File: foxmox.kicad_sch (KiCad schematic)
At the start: 0 parts

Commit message: Fully transcribed PDF scan
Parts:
- added C1, C2: 27pF, symbol Device:C_Small_US
- added C3: .1uF, symbol Device:C_Small_US
- added C4: 1uF, symbol Device:C_Small_US
- added D1: 6.2V, Diode_SMD:D_MiniMELF, symbol Diode:BZV55B6V2
- added P1: 2.5mm plug, symbol Connector_Audio:AudioJack3
- added Q1: 2N2222A, symbol Device:Q_NPN
- added R1, R3: 20k, symbol Device:R_US
- added R2: 5k, symbol Device:R_Potentiometer_Trim_US
- added R4: 2.7k, symbol Device:R_US
- added R5: 10k, symbol Device:R_US
- added S1, S2: SW Hex-4, Button_Switch_SMD:Nidec_Copal_SH-7040B, symbol Switch:SW_Coded_SH-7080
- added S3: SPDT, symbol Switch:SW_SPDT
- added U1: PIC16F84, symbol MCU_Microchip_PIC16:PIC16F84-XXP
- added Y1: 3.579MHz, symbol Device:Crystal
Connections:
- new net: Q1.B, R3.2
- new net: Q1.C, R4.1
- new net: C3.1, D1.1 (K), S3.2 (B), U1.14 (VDD), U1.4 (~{MCLR})
- new net: R5.2, U1.1 (RA2)
- new net: S2.1, U1.10 (RB4)
- new net: S2.2, U1.11 (RB5)
- new net: S2.4, U1.12 (RB6)
- new net: S2.8, U1.13 (RB7)
- new net: C2.1, U1.15 (OSC1/CLKIN), Y1.2
- new net: C1.1, U1.16 (OSC2/CLKOUT), Y1.1
- new net: R1.1, U1.17 (RA0)
- new net: R3.1, U1.18 (RA1)
- new net: R5.1, U1.2 (RA3)
- new net: S1.1, U1.6 (INT/RB0)
- new net: S1.2, U1.7 (RB1)
- new net: S1.4, U1.8 (RB2)
- new net: S1.8, U1.9 (RB3)
- new net: P1.R, S3.3 (C)
- new net: R1.2, R2.1
- new net: C4.1, R2.2
- new net: C4.2, P1.T, R4.2
- new net GNDREF: C1.2, C2.2, C3.2, D1.2 (A), P1.S, Q1.E, R2.3, S1.C, S2.C, S3.1 (A), U1.5 (VSS)
- no-connect marks 0 -> 1
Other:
- note added: "2.5mm stereo plug with molded cable cut to 3 in. long connecting to HT microphone input"
- note added: "Adjust for 20 to 40mV peak to peak. Or set R2 for ~300 ohms from wiper to ground."
- note added: "Measured current draw @ 3.0V from Ring to Sleeve = .5mA Idle .9mA transmitting"
- note added: "OFF"
- note added: "ON"
- note added: "This is a simplified version of the Fox Controller which is not programmable. Setting the 2 hex switches completely specifies the operation of the controller. Program these units with version 2.6 of the code."
- company: (none) -> Designed by Larry Benko, W0QE
- title: (none) -> Low Power FoxMOX Controller V.2.6

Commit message: Fix P1, should be a plug not a jack
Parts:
- removed P1: 2.5mm plug, symbol Connector_Audio:AudioJack3
- added P1: 2.5mm plug, symbol Connector_Audio:AudioPlug3
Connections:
- net GNDREF: now also P1.S
- net at S3.3 (C): now also P1.R
- net at C4.2, R4.2: now also P1.T
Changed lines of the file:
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@@
+	)
+	(symbol
+		(lib_id "Connector_Audio:AudioPlug3")
+		(at 48.26 49.53 0)
+		(mirror x)
+		(unit 1)
+		(body_style 1)
+		(exclude_from_sim no)
+		(in_bom yes)
+		(on_board yes)
+		(in_pos_files yes)
+		(dnp no)
+		(fields_autoplaced yes)
+		(property "Reference" "P1"
+			(at 34.29 48.2599 0)
+			(show_name no)
+			(do_not_autoplace no)
+			(effects
+				(font
+					(size 1.27 1.27)
+				)
+				(justify right)
+			)
+		)
+		(property "Value" "2.5mm plug"
+			(at 34.29 50.7999 0)
+			(show_name no)
+			(do_not_autoplace no)
+			(effects
+				(font
+					(size 1.27 1.27)
+				)
+				(justify right)
+			)
+		)
+		(property "Footprint" ""
+			(at 50.8 48.26 0)
+			(hide yes)
+			(show_name no)
+			(do_not_autoplace no)
+			(effects
+				(font
+					(size 1.27 1.27)
+				)
+			)
+		)
+		(property "Datasheet" ""
+			(at 50.8 48.26 0)
+			(hide yes)
+			(show_name no)
+			(do_not_autoplace no)
+			(effects
+				(font
+					(size 1.27 1.27)
+				)
+			)
+		)
+		(property "Description" "Audio Jack, 3 Poles (Stereo / TRS)"
+			(at 48.26 49.53 0)
+			(hide yes)
+			(show_name no)
+			(do_not_autoplace no)
+			(effects
+				(font
+					(size 1.27 1.27)
+				)
+			)
+		)
+		(pin "T"
+		)
+		(pin "S"
+		)
+		(pin "R"
+		)
+		(instances
+			(project "foxmox"
+				(path "/8fe0f122-3453-49de-aa82-6d9b89dc8357"
+					(reference "P1")
+					(unit 1)
+				)
+			)
+		)
 	)
 	(symbol
@@
 					(unit 1)
 				)
-			)
-		)
-	)
-	(symbol
-		(lib_id "Connector_Audio:AudioJack3")
-		(at 58.42 49.53 0)
-		(mirror x)
-		(unit 1)
-		(body_style 1)
-		(exclude_from_sim no)
-		(in_bom yes)
-		(on_board yes)
-		(in_pos_files yes)
-		(dnp no)
-		(fields_autoplaced yes)
-		(property "Reference" "P1"
-			(at 50.8 47.6249 0)
-			(show_name no)
-			(do_not_autoplace no)
-			(effects
-				(font
-					(size 1.27 1.27)
-				)
-				(justify right)
-			)
-		)
-		(property "Value" "2.5mm plug"
-			(at 50.8 50.1649 0)
-			(show_name no)
-			(do_not_autoplace no)
-			(effects
-				(font
-					(size 1.27 1.27)
-				)
-				(justify right)
-			)
-		)
-		(property "Footprint" ""
-			(at 58.42 49.53 0)
-			(hide yes)
-			(show_name no)
-			(do_not_autoplace no)
-			(effects
-				(font
-					(size 1.27 1.27)
-				)
-			)
-		)
-		(property "Datasheet" ""
-			(at 58.42 49.53 0)
-			(hide yes)
-			(show_name no)
-			(do_not_autoplace no)
-			(effects
-				(font
-					(size 1.27 1.27)
-				)
-			)
-		)
-		(property "Description" "Audio Jack, 3 Poles (Stereo / TRS)"
-			(at 58.42 49.53 0)
-			(hide yes)
-			(show_name no)
-			(do_not_autoplace no)
-			(effects
-				(font
-					(size 1.27 1.27)
-				)
-			)
-		)
-		(pin "T"
-		)
-		(pin "S"
-		)
-		(pin "R"
-		)
-		(instances
-			(project "foxmox"
-				(path "/8fe0f122-3453-49de-aa82-6d9b89dc8357"
-					(reference "P1")
-					(unit 1)
-				)

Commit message: Throw in some fake footprints and start PCB
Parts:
- C1, C2: footprint (none) -> Capacitor_THT:C_Disc_D3.0mm_W1.6mm_P2.50mm
- C3, C4: footprint (none) -> Capacitor_THT:CP_Radial_D8.0mm_P5.00mm
- P1: footprint (none) -> TerminalBlock:TerminalBlock_MaiXu_MX126-5.0-03P_1x03_P5.00mm
- Q1: footprint (none) -> Package_TO_SOT_THT:TO-92
- R1, R3, R4, R5: footprint (none) -> Resistor_THT:R_Axial_DIN0207_L6.3mm_D2.5mm_P15.24mm_Horizontal
- R2: footprint (none) -> Potentiometer_THT:Potentiometer_Piher_PT-15-H01_Horizontal
- S3: footprint (none) -> Button_Switch_THT:SW_E-Switch_EG1271_SPDT
- U1: footprint (none) -> Package_DIP:CERDIP-18_W7.62mm_SideBrazed
- Y1: footprint (none) -> Crystal:Crystal_HC52-6mm_Vertical
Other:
- title: Low Power FoxMOX Controller V.2.6 -> Low Power FoxMOX Controller

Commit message: Slightly better PCB
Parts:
- D1: footprint Diode_SMD:D_MiniMELF -> Diode_THT:D_A-405_P10.16mm_Horizontal
- P1: footprint TerminalBlock:TerminalBlock_MaiXu_MX126-5.0-03P_1x03_P5.00mm -> TerminalBlock_CUI:TerminalBlock_CUI_TB007-508-03_1x03_P5.08mm_Horizontal
- R2: footprint Potentiometer_THT:Potentiometer_Piher_PT-15-H01_Horizontal -> Potentiometer_THT:Potentiometer_Bourns_3266W_Vertical
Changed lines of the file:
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@@
 			)
 		)
-		(property "Footprint" "Diode_SMD:D_MiniMELF"
+		(property "Footprint" "Diode_THT:D_A-405_P10.16mm_Horizontal"
 			(at 33.655 91.44 0)
 			(hide yes)
@@
 			)
 		)
-		(property "Footprint" "Potentiometer_THT:Potentiometer_Piher_PT-15-H01_Horizontal"
+		(property "Footprint" "Potentiometer_THT:Potentiometer_Bourns_3266W_Vertical"
 			(at 123.19 72.39 0)
 			(hide yes)
@@
 			)
 		)
-		(property "Footprint" "TerminalBlock:TerminalBlock_MaiXu_MX126-5.0-03P_1x03_P5.00mm"
+		(property "Footprint" "TerminalBlock_CUI:TerminalBlock_CUI_TB007-508-03_1x03_P5.08mm_Horizontal"
 			(at 50.8 48.26 0)
 			(hide yes)

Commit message: Add datasheets and libraries for chosen components
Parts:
- added H1, H2, H3, H4: MountingHole, MountingHole:MountingHole_2.5mm, symbol Mechanical:MountingHole
- S1, S2: footprint Button_Switch_SMD:Nidec_Copal_SH-7040B -> RDS5_16S_1065_D_67:SW_RDS5-16S-1065-D-67; symbol Switch:SW_Coded_SH-7080 -> RDS5-16S-1065-D-67:RDS5-16S-1065-D-67; MANUFACTURER (none) -> CUI Devices; MAXIMUM_PACKAGE_HEIGHT (none) -> 6.8mm; PARTREV (none) -> 1.0; STANDARD (none) -> Manufacturer Recommendations
- S3: footprint Button_Switch_THT:SW_E-Switch_EG1271_SPDT -> Button_Switch_THT:SW_CK_JS202011CQN_DPDT_Straight
- Y1: footprint Crystal:Crystal_HC52-6mm_Vertical -> Crystal:Crystal_HC49-4H_Vertical
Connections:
- net GNDREF: now also S1.C1 (C), S1.C2 (C__1), S2.C1 (C), S2.C2 (C__1); no longer S1.C, S2.C

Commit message: Slightly thicker power traces
And possibly fix transistor pins
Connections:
- net VDD: now reaches C3.1, D1.1 (K), S3.2 (B), U1.14 (VDD), U1.4 (~{MCLR})
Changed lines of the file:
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@@
+		)
+	)
+	(label "VDD"
+		(at 63.5 80.01 0)
+		(effects
+			(font
+				(size 1.27 1.27)
+			)
+			(justify left bottom)
 		)
 	)

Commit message: Adjust some parts, footprints, etc
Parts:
- added TP1: VDD, TestPoint:TestPoint_Pad_D2.0mm, symbol Connector:TestPoint
- C1, C2: footprint Capacitor_THT:C_Disc_D3.0mm_W1.6mm_P2.50mm -> Capacitor_THT:C_Disc_D4.3mm_W1.9mm_P5.00mm
- C3, C4: footprint Capacitor_THT:CP_Radial_D8.0mm_P5.00mm -> Capacitor_THT:C_Disc_D4.3mm_W1.9mm_P5.00mm
- D1: footprint Diode_THT:D_A-405_P10.16mm_Horizontal -> Diode_THT:D_DO-35_SOD27_P7.62mm_Horizontal
- H1, H2, H3, H4: footprint MountingHole:MountingHole_2.5mm -> MountingHole:MountingHole_2.5mm_Pad; symbol Mechanical:MountingHole -> Mechanical:MountingHole_Pad
- Q1: footprint Package_TO_SOT_THT:TO-92 -> Package_TO_SOT_THT:TO-92_Inline_Wide
- S3: footprint Button_Switch_THT:SW_CK_JS202011CQN_DPDT_Straight -> EG1218:SW_1218_EWI
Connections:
- net GNDREF: now also H1.1, H2.1, H3.1, H4.1, Q1.1 (E); no longer Q1.E
- net VDD: now also TP1.1
- net at R3.2: now also Q1.2 (B); no longer Q1.B
- net at R4.1: now also Q1.3 (C); no longer Q1.C
- net at C2.1, Y1.2: now also U1.16 (OSC1/CLKIN); no longer U1.15 (OSC1/CLKIN)
- net at C1.1, Y1.1: now also U1.15 (OSC2/CLKOUT); no longer U1.16 (OSC2/CLKOUT)

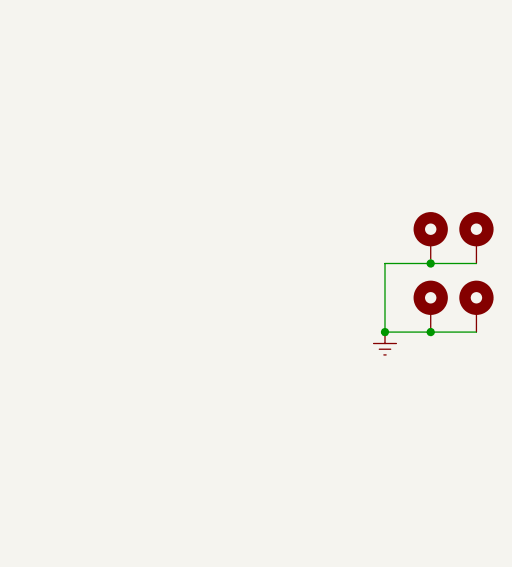
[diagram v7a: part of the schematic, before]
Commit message: Change 2.5mm terminal block and add strain relief
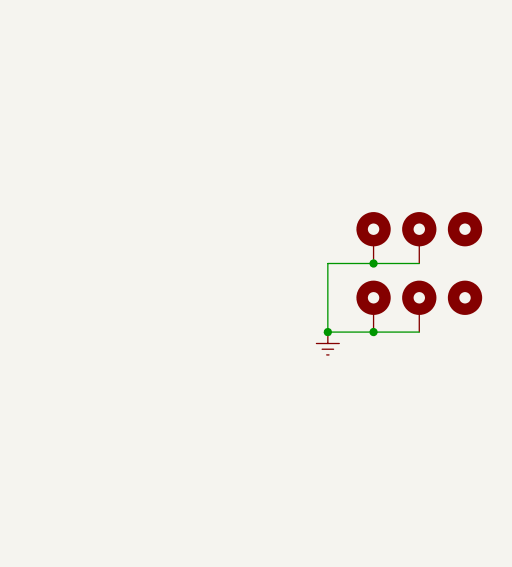
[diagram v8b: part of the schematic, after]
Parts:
- added H5, H6: MountingHole, MountingHole:MountingHole_2mm, symbol Mechanical:MountingHole
- C3, C4: footprint Capacitor_THT:C_Disc_D4.3mm_W1.9mm_P5.00mm -> Capacitor_THT:C_Disc_D7.5mm_W5.0mm_P7.50mm
- P1: footprint TerminalBlock_CUI:TerminalBlock_CUI_TB007-508-03_1x03_P5.08mm_Horizontal -> TerminalBlock:TerminalBlock_Xinya_XY308-2.54-3P_1x03_P2.54mm_Horizontal
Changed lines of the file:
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@@
 	)
 	(junction
-		(at 259.08 160.02)
+		(at 252.73 160.02)
 		(diameter 0)
 		(color 0 0 0 0)
 	)
 	(junction
-		(at 259.08 167.64)
+		(at 252.73 167.64)
 		(diameter 0)
 		(color 0 0 0 0)
@@
 	)
 	(junction
-		(at 254 167.64)
+		(at 247.65 167.64)
 		(diameter 0)
 		(color 0 0 0 0)
@@
 	(wire
 		(pts
-			(xy 259.08 160.02) (xy 264.16 160.02)
+			(xy 252.73 160.02) (xy 257.81 160.02)
 		)
 		(stroke
@@
 	(wire
 		(pts
-			(xy 254 160.02) (xy 254 167.64)
+			(xy 247.65 160.02) (xy 247.65 167.64)
 		)
 		(stroke
@@
 	(wire
 		(pts
-			(xy 259.08 167.64) (xy 264.16 167.64)
+			(xy 252.73 167.64) (xy 257.81 167.64)
 		)
 		(stroke
@@
 	(wire
 		(pts
-			(xy 259.08 160.02) (xy 254 160.02)
+			(xy 252.73 160.02) (xy 247.65 160.02)
 		)
 		(stroke
@@
 	(wire
 		(pts
-			(xy 254 167.64) (xy 259.08 167.64)
+			(xy 247.65 167.64) (xy 252.73 167.64)
 		)
 		(stroke
@@
 			)
 		)
-		(property "Footprint" "Capacitor_THT:C_Disc_D4.3mm_W1.9mm_P5.00mm"
+		(property "Footprint" "Capacitor_THT:C_Disc_D7.5mm_W5.0mm_P7.50mm"
 			(at 48.26 91.44 0)
 			(hide yes)
@@
 	(symbol
 		(lib_id "power:GNDREF")
-		(at 254 167.64 0)
+		(at 247.65 167.64 0)
 		(unit 1)
 		(body_style 1)
@@
 		(fields_autoplaced yes)
 		(property "Reference" "#PWR011"
-			(at 254 173.99 0)
+			(at 247.65 173.99 0)
 			(hide yes)
 			(show_name no)
@@
 		)
 		(property "Value" "GNDREF"
-			(at 254 172.72 0)
+			(at 247.65 172.72 0)
 			(hide yes)
 			(show_name no)
@@
 		)
 		(property "Footprint" ""
-			(at 254 167.64 0)
+			(at 247.65 167.64 0)
 			(hide yes)
 			(show_name no)
@@
 		)
 		(property "Datasheet" ""
-			(at 254 167.64 0)
+			(at 247.65 167.64 0)
 			(hide yes)
 			(show_name no)
@@
 		)
 		(property "Description" "Power symbol creates a global label with name \"GNDREF\" , reference supply ground"
-			(at 254 167.64 0)
+			(at 247.65 167.64 0)
 			(hide yes)
 			(show_name no)
@@
 	)
 	(symbol
+		(lib_id "Mechanical:MountingHole")
+		(at 262.89 156.21 0)
+		(unit 1)
+		(body_style 1)
+		(exclude_from_sim no)
+		(in_bom no)
+		(on_board yes)
+		(in_pos_files yes)
+		(dnp no)
+		(fields_autoplaced yes)
+		(property "Reference" "H5"
+			(at 265.43 154.9399 0)
+			(hide yes)
+			(show_name no)
+			(do_not_autoplace no)
+			(effects
+				(font
+					(size 1.27 1.27)
+				)
+				(justify left)
+			)
+		)
+		(property "Value" "MountingHole"
+			(at 265.43 157.4799 0)
+			(hide yes)
+			(show_name no)
+			(do_not_autoplace no)
+			(effects
+				(font
+					(size 1.27 1.27)
+				)
+				(justify left)
+			)
+		)
+		(property "Footprint" "MountingHole:MountingHole_2mm"
+			(at 262.89 156.21 0)
+			(hide yes)
+			(show_name no)
+			(do_not_autoplace no)
+			(effects
+				(font
+					(size 1.27 1.27)
+				)
+			)
+		)
+		(property "Datasheet" ""
+			(at 262.89 156.21 0)
+			(hide yes)
+			(show_name no)
+			(do_not_autoplace no)
+			(effects
+				(font
+					(size 1.27 1.27)
+				)
+			)
+		)
+		(property "Description" "Mounting Hole without connection"
+			(at 262.89 156.21 0)
+			(hide yes)
+			(show_name no)
+			(do_not_autoplace no)
+			(effects
+				(font
+					(size 1.27 1.27)
+				)
+			)
+		)
+		(instances
+			(project "foxmox"
+				(path "/8fe0f122-3453-49de-aa82-6d9b89dc8357"
+					(reference "H5")
+					(unit 1)
+				)
+			)
+		)
+	)
+	(symbol
 		(lib_id "Mechanical:MountingHole_Pad")
-		(at 264.16 165.1 0)
+		(at 257.81 165.1 0)
 		(unit 1)
 		(body_style 1)
@@
 		(fields_autoplaced yes)
 		(property "Reference" "H4"
-			(at 266.7 163.8299 0)
+			(at 260.35 163.8299 0)
 			(hide yes)
 			(show_name no)
@@
 		)
 		(property "Value" "MountingHole"
-			(at 266.7 166.3699 0)
+			(at 260.35 166.3699 0)
 			(hide yes)
 			(show_name no)
@@
 		)
 		(property "Footprint" "MountingHole:MountingHole_2.5mm_Pad"
-			(at 264.16 165.1 0)
+			(at 257.81 165.1 0)
 			(hide yes)
 			(show_name no)
@@
 		)
 		(property "Datasheet" ""
-			(at 264.16 165.1 0)
+			(at 257.81 165.1 0)
 			(hide yes)
 			(show_name no)
@@
 		)
 		(property "Description" "Mounting Hole with connection"
-			(at 264.16 165.1 0)
+			(at 257.81 165.1 0)
 			(hide yes)
 			(show_name no)
@@
 	)
 	(symbol
+		(lib_id "Mechanical:MountingHole")
+		(at 262.89 163.83 0)
+		(unit 1)
+		(body_style 1)
+		(exclude_from_sim no)
+		(in_bom no)
+		(on_board yes)
+		(in_pos_files yes)
+		(dnp no)
+		(fields_autoplaced yes)
+		(property "Reference" "H6"
+			(at 265.43 162.5599 0)
+			(hide yes)
+			(show_name no)
+			(do_not_autoplace no)
+			(effects
+				(font
+					(size 1.27 1.27)
+				)
+				(justify left)
+			)
+		)
+		(property "Value" "MountingHole"
+			(at 265.43 165.0999 0)
+			(hide yes)
+			(show_name no)
+			(do_not_autoplace no)
+			(effects
+				(font
+					(size 1.27 1.27)
+				)
+				(justify left)
+			)
+		)
+		(property "Footprint" "MountingHole:MountingHole_2mm"
+			(at 262.89 163.83 0)
+			(hide yes)
+			(show_name no)
+			(do_not_autoplace no)
+			(effects
+				(font
+					(size 1.27 1.27)
+				)
+			)
+		)
+		(property "Datasheet" ""
+			(at 262.89 163.83 0)
+			(hide yes)
+			(show_name no)
+			(do_not_autoplace no)
+			(effects
+				(font
+					(size 1.27 1.27)
+				)
+			)
+		)
+		(property "Description" "Mounting Hole without connection"
+			(at 262.89 163.83 0)
+			(hide yes)
+			(show_name no)
+			(do_not_autoplace no)
+			(effects
+				(font
+					(size 1.27 1.27)
+				)
+			)
+		)
+		(instances
+			(project "foxmox"
+				(path "/8fe0f122-3453-49de-aa82-6d9b89dc8357"
+					(reference "H6")
+					(unit 1)
+				)
+			)
+		)
+	)
+	(symbol
 		(lib_id "Connector_Audio:AudioPlug3")
 		(at 48.26 49.53 0)
@@
 			)
 		)
-		(property "Footprint" "TerminalBlock_CUI:TerminalBlock_CUI_TB007-508-03_1x03_P5.08mm_Horizontal"
+		(property "Footprint" "TerminalBlock:TerminalBlock_Xinya_XY308-2.54-3P_1x03_P2.54mm_Horizontal"
 			(at 50.8 48.26 0)
 			(hide yes)
@@
 			)
 		)
-		(property "Footprint" "Capacitor_THT:C_Disc_D4.3mm_W1.9mm_P5.00mm"
+		(property "Footprint" "Capacitor_THT:C_Disc_D7.5mm_W5.0mm_P7.50mm"
 			(at 134.62 72.39 0)
 			(hide yes)
@@
 	(symbol
 		(lib_id "Mechanical:MountingHole_Pad")
-		(at 259.08 157.48 0)
+		(at 252.73 157.48 0)
 		(unit 1)
 		(body_style 1)
@@
 		(fields_autoplaced yes)
 		(property "Reference" "H1"
-			(at 261.62 156.2099 0)
+			(at 255.27 156.2099 0)
 			(hide yes)
 			(show_name no)
@@
 		)
 		(property "Value" "MountingHole"
-			(at 261.62 158.7499 0)
+			(at 255.27 158.7499 0)
 			(hide yes)
 			(show_name no)
@@
 		)
 		(property "Footprint" "MountingHole:MountingHole_2.5mm_Pad"
-			(at 259.08 157.48 0)
+			(at 252.73 157.48 0)
 			(hide yes)
 			(show_name no)
@@
 		)
 		(property "Datasheet" ""
-			(at 259.08 157.48 0)
+			(at 252.73 157.48 0)
 			(hide yes)
 			(show_name no)
@@
 		)
 		(property "Description" "Mounting Hole with connection"
-			(at 259.08 157.48 0)
+			(at 252.73 157.48 0)
 			(hide yes)
 			(show_name no)
@@
 	(symbol
 		(lib_id "Mechanical:MountingHole_Pad")
-		(at 264.16 157.48 0)
+		(at 257.81 157.48 0)
 		(unit 1)
 		(body_style 1)
@@
 		(fields_autoplaced yes)
 		(property "Reference" "H2"
-			(at 266.7 156.2099 0)
+			(at 260.35 156.2099 0)
 			(hide yes)
 			(show_name no)
@@
 		)
 		(property "Value" "MountingHole"
-			(at 266.7 158.7499 0)
+			(at 260.35 158.7499 0)
 			(hide yes)
 			(show_name no)
@@
 		)
 		(property "Footprint" "MountingHole:MountingHole_2.5mm_Pad"
-			(at 264.16 157.48 0)
+			(at 257.81 157.48 0)
 			(hide yes)
 			(show_name no)
@@
 		)
 		(property "Datasheet" ""
-			(at 264.16 157.48 0)
+			(at 257.81 157.48 0)
 			(hide yes)
 			(show_name no)
@@
 		)
 		(property "Description" "Mounting Hole with connection"
-			(at 264.16 157.48 0)
+			(at 257.81 157.48 0)
 			(hide yes)
 			(show_name no)
@@
 	(symbol
 		(lib_id "Mechanical:MountingHole_Pad")
-		(at 259.08 165.1 0)
+		(at 252.73 165.1 0)
 		(unit 1)
 		(body_style 1)
@@
 		(fields_autoplaced yes)
 		(property "Reference" "H3"
-			(at 261.62 163.8299 0)
+			(at 255.27 163.8299 0)
 			(hide yes)
 			(show_name no)
@@
 		)
 		(property "Value" "MountingHole"
-			(at 261.62 166.3699 0)
+			(at 255.27 166.3699 0)
 			(hide yes)
 			(show_name no)
@@
 		)
 		(property "Footprint" "MountingHole:MountingHole_2.5mm_Pad"
-			(at 259.08 165.1 0)
+			(at 252.73 165.1 0)
 			(hide yes)
 			(show_name no)
@@
 		)
 		(property "Datasheet" ""
-			(at 259.08 165.1 0)
+			(at 252.73 165.1 0)
 			(hide yes)
 			(show_name no)
@@
 		)
 		(property "Description" "Mounting Hole with connection"
-			(at 259.08 165.1 0)
+			(at 252.73 165.1 0)
 			(hide yes)
 			(show_name no)
